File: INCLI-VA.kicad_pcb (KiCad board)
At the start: 2 copper layers, 100 x 70 mm, 155 parts, among them J1 MSTB 2,5/5-GF-5,08, J2 MSTB 2,5/2-GF-5,08, J401 USB4105-GF-A, J402 UART0, Q101 STD18NF25, Q102 IPD30N10S3L-34, Q701 FDD7N25LZ, Q702 BC817-40, Q703 BC807-40, Q751 FDD7N25LZ, Q752 BC817-40, Q753 BC807-40, SW401 RESET, SW402 BOOT, U1 ADM3055E, U101 LM74930QRGERQ1, U201 TPS7A1650QDGNRQ1, U202 ISO7763FQDWRQ1, U301 TPS62A02QDRLRQ1, U302 LP5907QMFX-3.3Q1, U401 ESP32-S3-WROOM-1-N8R2, U402 USBLC6-2SC6, U501 SCL3300-D01, U502 ASM330LHHTR, U503 AS5147U-HTSM

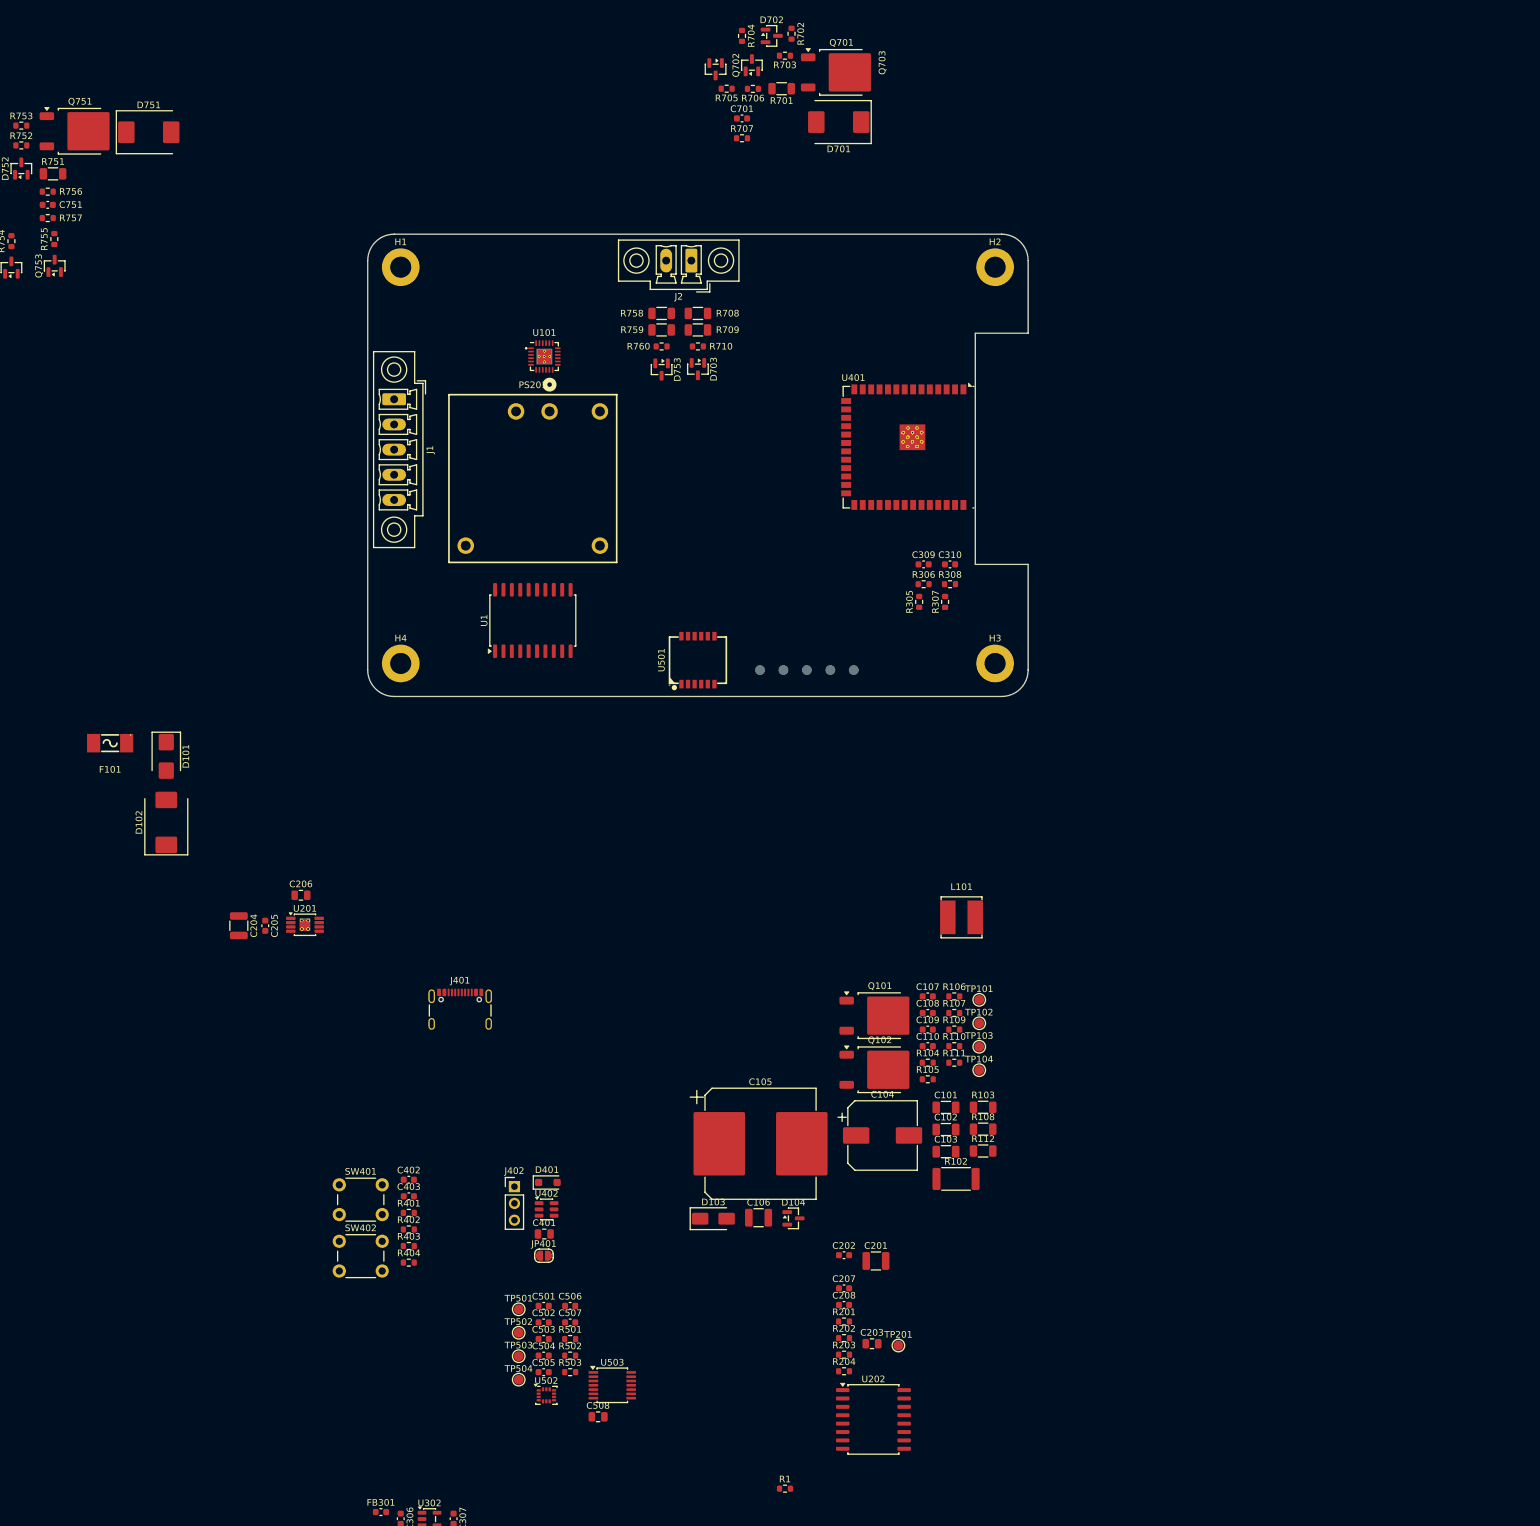
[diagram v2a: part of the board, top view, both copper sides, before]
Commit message: PCB: Update PCB from Schematic (hecho por el usuario en KiCad, F8)
Vinculado por UUID, con reemplazo de huellas y sin actualizar desde la
librería. Entran las hojas 60/70/80 y el buck de 20; salen PS201, U202 y
los pasivos de la opción aislada. Efecto colateral: se borraron los
agujeros de montaje H1-H4, que solo estaban en el PCB.

Co-Authored-By: Claude Opus 5.5 <noreply@anthropic.com>
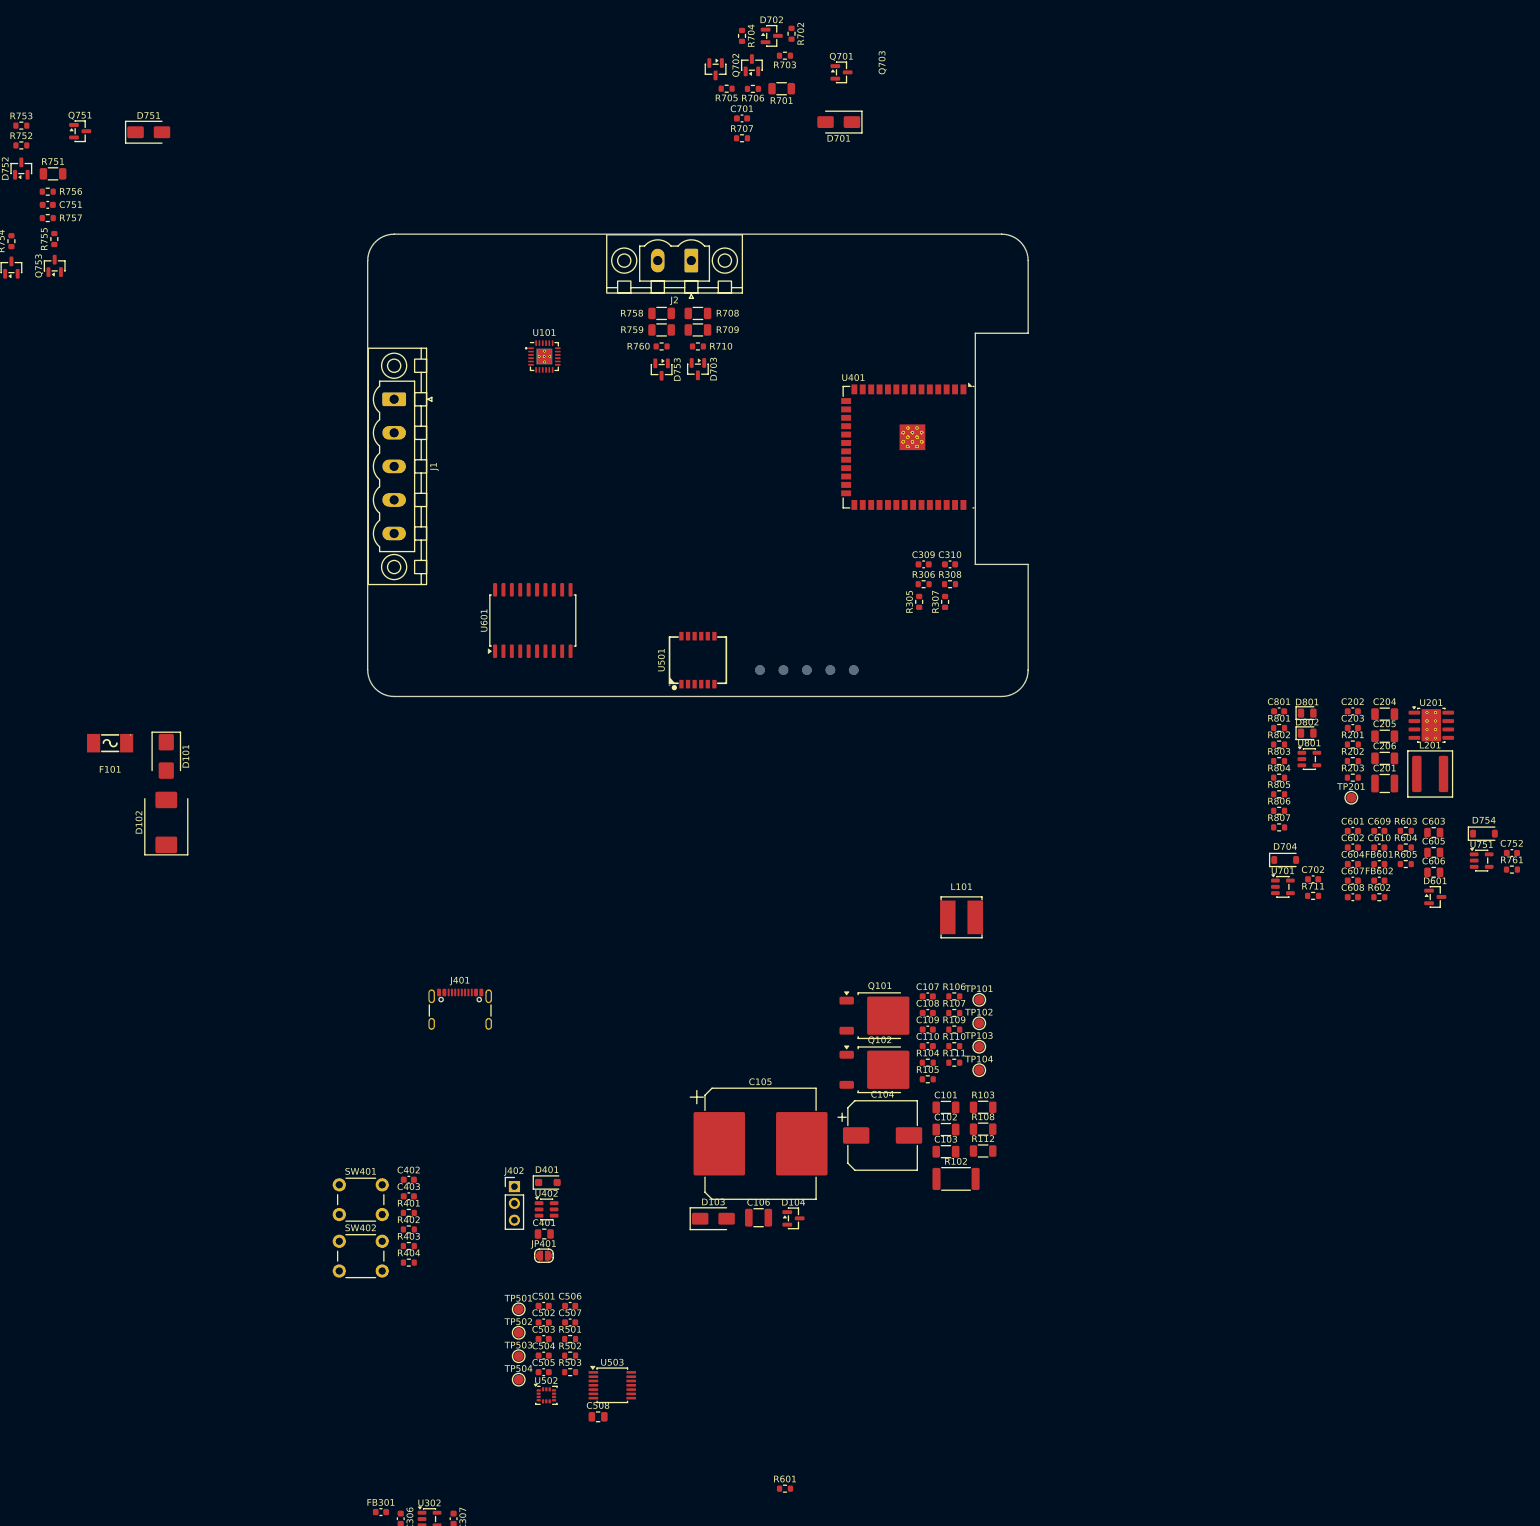
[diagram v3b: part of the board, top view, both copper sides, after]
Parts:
- removed C207, C208: 100nF, Capacitor_SMD:C_0603_1608Metric
- removed H1, H2, H3, H4: MountingHole_3.2mm_M3_ISO7380_Pad, MountingHole:MountingHole_3.2mm_M3_ISO7380_Pad
- removed PS201: URB2405YMD-10WR3, INCLI-VA:PWRM-TH_URBXXXXYMD_10WR3
- removed R204: 100k, Resistor_SMD:R_0603_1608Metric
- removed U202: ISO7763FQDWRQ1, Package_SO:SOIC-16W_7.5x10.3mm_P1.27mm
- added C601: 10nF, Capacitor_SMD:C_0603_1608Metric, F.Cu at (249.2, 140.4)
- added C602: 100nF, Capacitor_SMD:C_0603_1608Metric, F.Cu at (249.2, 142.9)
- added C603: 10uF, Capacitor_SMD:C_0805_2012Metric, F.Cu at (261.4, 140.6)
- added C604: 100nF, Capacitor_SMD:C_0603_1608Metric, F.Cu at (249.2, 145.4)
- added C605: 10uF, Capacitor_SMD:C_0805_2012Metric, F.Cu at (261.4, 143.6)
- added C606: 10uF, Capacitor_SMD:C_0805_2012Metric, F.Cu at (261.4, 146.6)
- added C607: 10nF, Capacitor_SMD:C_0603_1608Metric, F.Cu at (249.2, 147.9)
- added C608: 100nF, Capacitor_SMD:C_0603_1608Metric, F.Cu at (249.2, 150.4)
- added C609: 4.7nF, Capacitor_SMD:C_0603_1608Metric, F.Cu at (253.2, 140.4)
- added C610: 220nF, Capacitor_SMD:C_0603_1608Metric, F.Cu at (253.2, 142.9)
- added C702: 100nF, Capacitor_SMD:C_0603_1608Metric, F.Cu at (243.2, 147.7)
- added C752: 100nF, Capacitor_SMD:C_0603_1608Metric, F.Cu at (273.3, 143.7)
- added C801: 100nF, Capacitor_SMD:C_0603_1608Metric, F.Cu at (238.0, 122.3)
- added D601: ESD2CAN24-Q1, Package_TO_SOT_SMD:SOT-23, F.Cu at (261.6, 150.4)
- added D704: 12V, Diode_SMD:D_SOD-123, F.Cu at (238.9, 144.8)
- added D754: 12V, Diode_SMD:D_SOD-123, F.Cu at (269.0, 140.8)
- added D801: verde, LED_SMD:LED_0805_2012Metric, F.Cu at (242.3, 122.5)
- added D802: rojo, LED_SMD:LED_0805_2012Metric, F.Cu at (242.3, 125.6)
- added FB601: 1.8k@100MHz, Inductor_SMD:L_0603_1608Metric, F.Cu at (253.2, 145.4)
- added FB602: 1.8k@100MHz, Inductor_SMD:L_0603_1608Metric, F.Cu at (253.2, 147.9)
- added L201: 33uH, Inductor_SMD:L_Coilcraft_XAL6060-XXX, F.Cu at (260.9, 131.7)
- added R602: 60.4, Resistor_SMD:R_0603_1608Metric, F.Cu at (253.2, 150.4)
- added R603: 60.4, Resistor_SMD:R_0603_1608Metric, F.Cu at (257.2, 140.4)
- added R604: 10k, Resistor_SMD:R_0603_1608Metric, F.Cu at (257.2, 142.9)
- added R605: 0, Resistor_SMD:R_0603_1608Metric, F.Cu at (257.2, 145.4)
- added R711: 100k, Resistor_SMD:R_0603_1608Metric, F.Cu at (243.2, 150.2)
- added R761: 100k, Resistor_SMD:R_0603_1608Metric, F.Cu at (273.3, 146.2)
- added R801: 1k, Resistor_SMD:R_0603_1608Metric, F.Cu at (238.0, 124.8)
- added R802: 0, Resistor_SMD:R_0603_1608Metric, F.Cu at (238.0, 127.3)
- added R803: 470, Resistor_SMD:R_0603_1608Metric, F.Cu at (238.0, 129.8)
- added R804: 470, Resistor_SMD:R_0603_1608Metric, F.Cu at (238.0, 132.3)
- added R805: 0, Resistor_SMD:R_0603_1608Metric, F.Cu at (238.0, 134.8)
- added R806: 0, Resistor_SMD:R_0603_1608Metric, F.Cu at (238.0, 137.3)
- added R807: 0, Resistor_SMD:R_0603_1608Metric, F.Cu at (238.0, 139.8)
- added U701: 74AHCT1G126, Package_TO_SOT_SMD:SOT-23-5, F.Cu at (238.6, 148.8)
- added U751: 74AHCT1G126, Package_TO_SOT_SMD:SOT-23-5, F.Cu at (268.7, 144.8)
- added U801: TPS3828-33Q1, Package_TO_SOT_SMD:SOT-23-5, F.Cu at (242.6, 129.5)
- C105: value 1000uF DNP -> 1000uF
- C109: value 10nF -> 100nF
- C201: value 2.2uF -> 4.7uF
- C203: value 10uF -> 100nF; footprint Capacitor_SMD:C_0805_2012Metric -> Capacitor_SMD:C_0603_1608Metric
- C204: value 2.2uF -> 22uF; footprint Capacitor_SMD:C_1210_3225Metric -> Capacitor_SMD:C_1206_3216Metric
- C205: value 100nF -> 22uF; footprint Capacitor_SMD:C_0603_1608Metric -> Capacitor_SMD:C_1206_3216Metric
- C206: value 10uF -> 22uF; footprint Capacitor_SMD:C_0805_2012Metric -> Capacitor_SMD:C_1206_3216Metric
- D701, D751: value SMCJ188A -> SMAJ58A; footprint Diode_SMD:D_SMC -> Diode_SMD:D_SMA
- D703, D753: value BZX84-C5V1 -> BZX84-C3V3
- J1: value MSTB 2,5/5-GF-5,08 -> MSTBV 2,5/5-GF-5,08; footprint Connector_Phoenix_MC:PhoenixContact_MCV_1,5_5-GF-3.81_1x05_P3.81mm_Vertical_ThreadedFlange -> Connector_Phoenix_MSTB:PhoenixContact_MSTBV_2,5_5-GF-5,08_1x05_P5.08mm_Vertical_ThreadedFlange
- J2: value MSTB 2,5/2-GF-5,08 -> MSTBV 2,5/2-GF-5,08; footprint Connector_Phoenix_MC:PhoenixContact_MCV_1,5_2-GF-3.81_1x02_P3.81mm_Vertical_ThreadedFlange -> Connector_Phoenix_MSTB:PhoenixContact_MSTBV_2,5_2-GF-5,08_1x02_P5.08mm_Vertical_ThreadedFlange
- Q701, Q751: value FDD7N25LZ -> DMN10H220LQ; footprint Package_TO_SOT_SMD:TO-252-2 -> Package_TO_SOT_SMD:SOT-23
- R202: value 100k -> 24.9k
- R203: value 100k -> 64.9k
- TP301: value +5V_ISO -> +5V_VEH
- TP304: value GND_ISO -> GND_VEH
- U201: value TPS7A1650QDGNRQ1 -> LMR38010SQDDARQ1; footprint Package_SO:HVSSOP-8-1EP_3x3mm_P0.65mm_EP1.57x1.89mm_ThermalVias -> Package_SO:SOIC-8-1EP_3.9x4.9mm_P1.27mm_EP2.95x4.9mm_Mask2.71x3.4mm_ThermalVias
- moved C204 176.4 mm to (254.0, 122.7), turned to 0 degrees
- moved U201 173.2 mm to (261.0, 124.4)
- moved C205 171.9 mm to (254.0, 126.0), turned to 0 degrees
- moved C206 165.4 mm to (254.0, 129.4)
- moved C203 118.3 mm to (249.2, 124.8)
- moved R201 116.5 mm to (249.2, 127.3)
- moved R202 116.5 mm to (249.2, 129.8)
- moved R203 116.5 mm to (249.2, 132.3)
- moved C202 112.8 mm to (249.2, 122.3)
- moved TP201 107.6 mm to (248.9, 135.3)
- moved C201 105.7 mm to (254.0, 133.2)
- renumbered R1 to R601, U1 to U601
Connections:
- C203 pad 1: +5V_ISO -> /20_buck_5v/BUCK_BOOT
- C203 pad 2: GND_ISO -> /20_buck_5v/BUCK_SW
- C204 pad 1: +VPROT -> +5V_VEH
- C205 pad 1: +VPROT -> +5V_VEH
- C301 pad 1: +5V_ISO -> +5V_VEH
- C301 pad 2: GND_ISO -> GND_VEH
- C302 pad 1: +5V_ISO -> +5V_VEH
- C302 pad 2: GND_ISO -> GND_VEH
- C304 pad 2: GND_ISO -> GND_VEH
- C306 pad 2: GND_ISO -> GND_VEH
- C307 pad 2: GND_ISO -> GND_VEH
- C309 pad 2: GND_ISO -> GND_VEH
- C310 pad 2: GND_ISO -> GND_VEH
- C401 pad 2: GND_ISO -> GND_VEH
- C402 pad 2: GND_ISO -> GND_VEH
- C403 pad 2: GND_ISO -> GND_VEH
- C501 pad 2: GND_ISO -> GND_VEH
- C502 pad 2: GND_ISO -> GND_VEH
- C503 pad 2: GND_ISO -> GND_VEH
- C504 pad 2: GND_ISO -> GND_VEH
- C505 pad 2: GND_ISO -> GND_VEH
- C506 pad 2: GND_ISO -> GND_VEH
- C507 pad 2: GND_ISO -> GND_VEH
- C508 pad 2: GND_ISO -> GND_VEH
- D702 pad 1: /VEH_PWR_FLT_N -> /PWR_FLT_N
- D703 pad 3: /VEH_DO1_DIAG -> /DO1_DIAG
- D752 pad 1: /VEH_PWR_FLT_N -> /PWR_FLT_N
- D753 pad 3: /VEH_DO2_DIAG -> /DO2_DIAG
- FB301 pad 1: +5V_ISO -> +5V_VEH
- J401 pad A1: GND_ISO -> GND_VEH
- J401 pad A12: GND_ISO -> GND_VEH
- J401 pad B1: GND_ISO -> GND_VEH
- J401 pad B12: GND_ISO -> GND_VEH
- J401 pad SH: GND_ISO -> GND_VEH
- J402 pad 3: GND_ISO -> GND_VEH
- JP401 pad 1: +5V_ISO -> +5V_VEH
- Q701 pad 2: /VEH_DO1 -> /70_output_DO1/SENSE
- Q701 pad 3: /70_output_DO1/SENSE -> /VEH_DO1
- Q703 pad 2: /VEH_DO1_EN -> /70_output_DO1/EN_5V
- Q751 pad 2: /VEH_DO2 -> /70_output_DO2/SENSE
- Q751 pad 3: /70_output_DO2/SENSE -> /VEH_DO2
- Q753 pad 2: /VEH_DO2_EN -> /70_output_DO2/EN_5V
- R111 pad 1: +5V_VEH -> +3V3_D
- R111 pad 2: /VEH_PWR_FLT_N -> /PWR_FLT_N
- R201 pad 1: /VEH_DO1_EN -> +5V_VEH
- R201 pad 2: GND_VEH -> /20_buck_5v/BUCK_FB
- R202 pad 1: /VEH_DO2_EN -> /20_buck_5v/BUCK_FB
- R203 pad 1: /DO1_EN -> /20_buck_5v/BUCK_RT
- R203 pad 2: GND_ISO -> GND_VEH
- R301 pad 1: +5V_ISO -> +5V_VEH
- R304 pad 2: GND_ISO -> GND_VEH
- R305 pad 1: +5V_ISO -> +5V_VEH
- R306 pad 2: GND_ISO -> GND_VEH
- R308 pad 2: GND_ISO -> GND_VEH
- R403 pad 2: GND_ISO -> GND_VEH
- R404 pad 2: GND_ISO -> GND_VEH
- R601 pad 2: GND_ISO -> GND_VEH
- R702 pad 1: /VEH_DO1_EN -> /70_output_DO1/EN_5V
- R704 pad 1: /VEH_DO1_EN -> /70_output_DO1/EN_5V
- R709 pad 2: /VEH_DO1_DIAG -> /DO1_DIAG
- R710 pad 1: /VEH_DO1_DIAG -> /DO1_DIAG
- R752 pad 1: /VEH_DO2_EN -> /70_output_DO2/EN_5V
- R754 pad 1: /VEH_DO2_EN -> /70_output_DO2/EN_5V
- R759 pad 2: /VEH_DO2_DIAG -> /DO2_DIAG
- R760 pad 1: /VEH_DO2_DIAG -> /DO2_DIAG
- SW401 pad 1: GND_ISO -> GND_VEH
- SW402 pad 1: GND_ISO -> GND_VEH
- TP104 pad 1: /VEH_PWR_FLT_N -> /PWR_FLT_N
- TP301 pad 1: +5V_ISO -> +5V_VEH
- TP304 pad 1: GND_ISO -> GND_VEH
- U101 pad 12: /VEH_PWR_FLT_N -> /PWR_FLT_N
- U201 pad 1: +5V_VEH -> GND_VEH
- U201 pad 2: unconnected-(U201-FB/NC-Pad2) -> +VPROT
- U201 pad 3: unconnected-(U201-PG-Pad3) -> +VPROT
- U201 pad 4: GND_VEH -> /20_buck_5v/BUCK_RT
- U201 pad 5: +VPROT -> /20_buck_5v/BUCK_FB
- U201 pad 7: unconnected-(U201-DELAY-Pad7) -> /20_buck_5v/BUCK_BOOT
- U201 pad 8: +VPROT -> /20_buck_5v/BUCK_SW
- U301 pad 1: GND_ISO -> GND_VEH
- U301 pad 3: +5V_ISO -> +5V_VEH
- U302 pad 2: GND_ISO -> GND_VEH
- U401 pad 1: GND_ISO -> GND_VEH
- U401 pad 11: /WD_EN -> unconnected-(U401-IO18-Pad11)
- U401 pad 12: unconnected-(U401-IO8-Pad12) -> /VAR_ID2
- U401 pad 40: GND_ISO -> GND_VEH
- U401 pad 41: GND_ISO -> GND_VEH
- U402 pad 2: GND_ISO -> GND_VEH
- U501 pad 1: GND_ISO -> GND_VEH
- U501 pad 11: GND_ISO -> GND_VEH
- U501 pad 12: GND_ISO -> GND_VEH
- U501 pad 3: GND_ISO -> GND_VEH
- U502 pad 2: GND_ISO -> GND_VEH
- U502 pad 3: GND_ISO -> GND_VEH
- U502 pad 6: GND_ISO -> GND_VEH
- U502 pad 7: GND_ISO -> GND_VEH
- U503 pad 13: GND_ISO -> GND_VEH
- U503 pad 5: GND_ISO -> GND_VEH
- U601 pad 1: GND_ISO -> GND_VEH
- U601 pad 10: GND_ISO -> GND_VEH
- U601 pad 12: unconnected-(U1-RS-Pad12) -> /60_can/CAN_RS
- U601 pad 18: GND_CAN -> /60_can/GNDISO_CAN
- U601 pad 2: GND_ISO -> GND_VEH
- U601 pad 20: GND_CAN -> /60_can/GNDISO_CAN
- U601 pad 3: +5V_ISO -> +5V_VEH
- U601 pad 9: unconnected-(U1-AUX_{IN}-Pad9) -> GND_VEH
